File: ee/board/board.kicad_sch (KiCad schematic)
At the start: 53 parts, among them J1 Conn_02x05_Odd_Even, J2 USB_A, J3 Micro_SD_Card_Det_Hirose_DM3AT, J4 Conn_01x08_Pin, J5 Conn_01x10_Pin, J6 Conn_Coaxial, SW1 SW_Push, U2 JW5211, U3 JW5211, U4 F1C100s, U5 SST26VF080A-104I/SN, U6 USBLC6-2SC6, Y1 Crystal_GND24

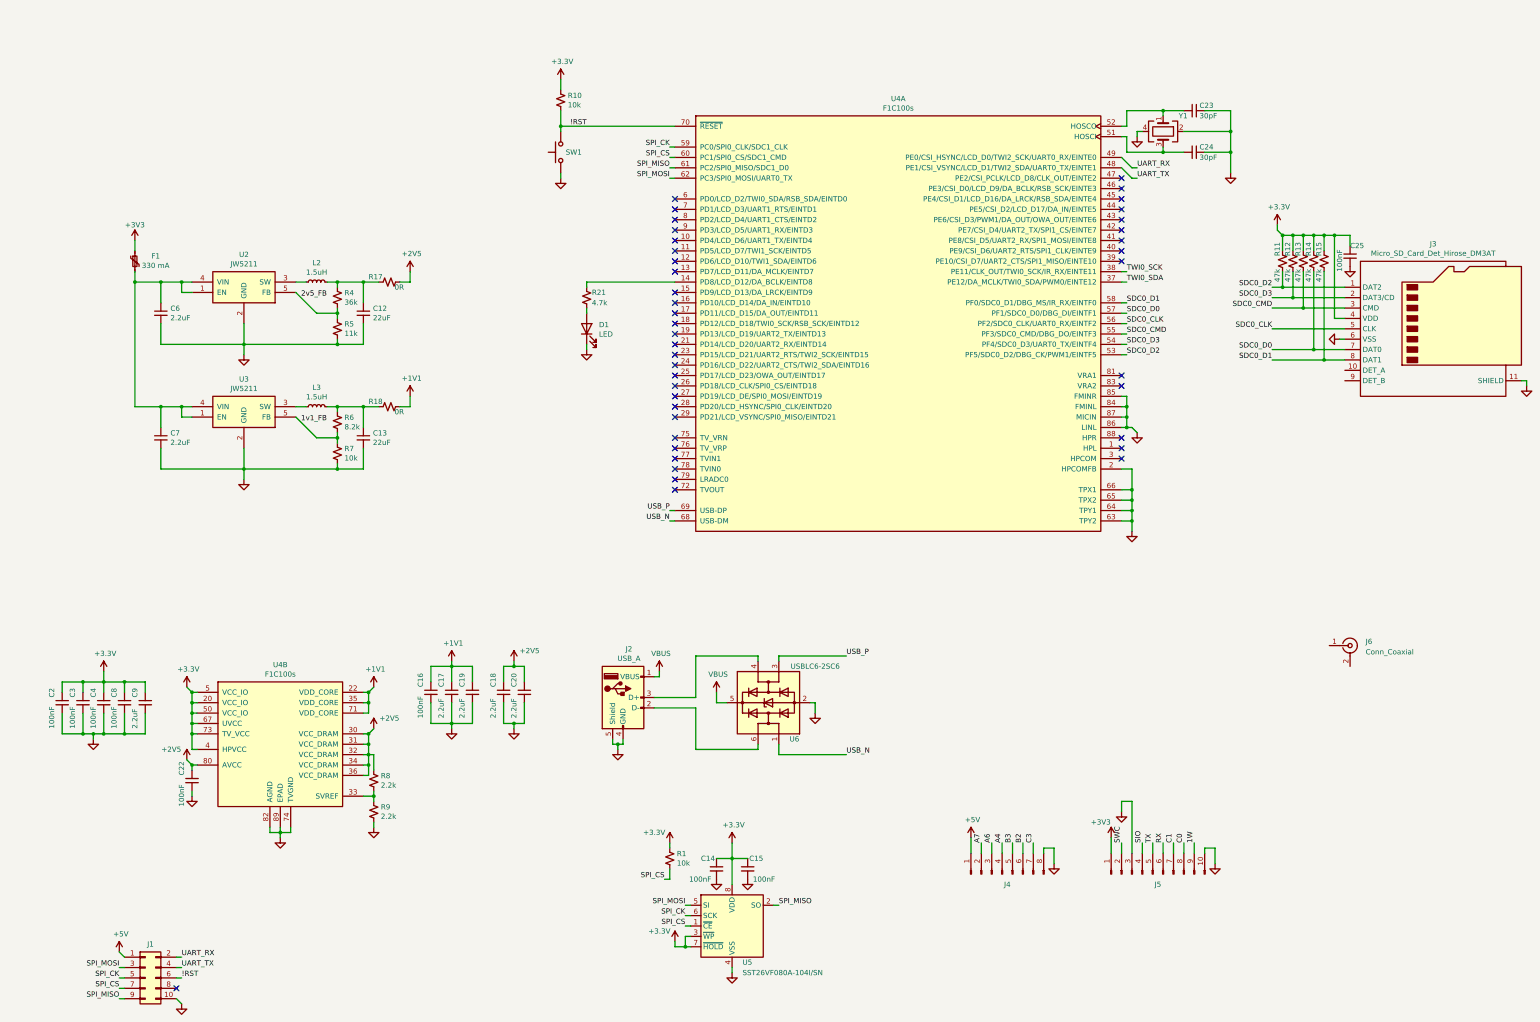
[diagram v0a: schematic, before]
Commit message: Dropped in the M.2 connectors.
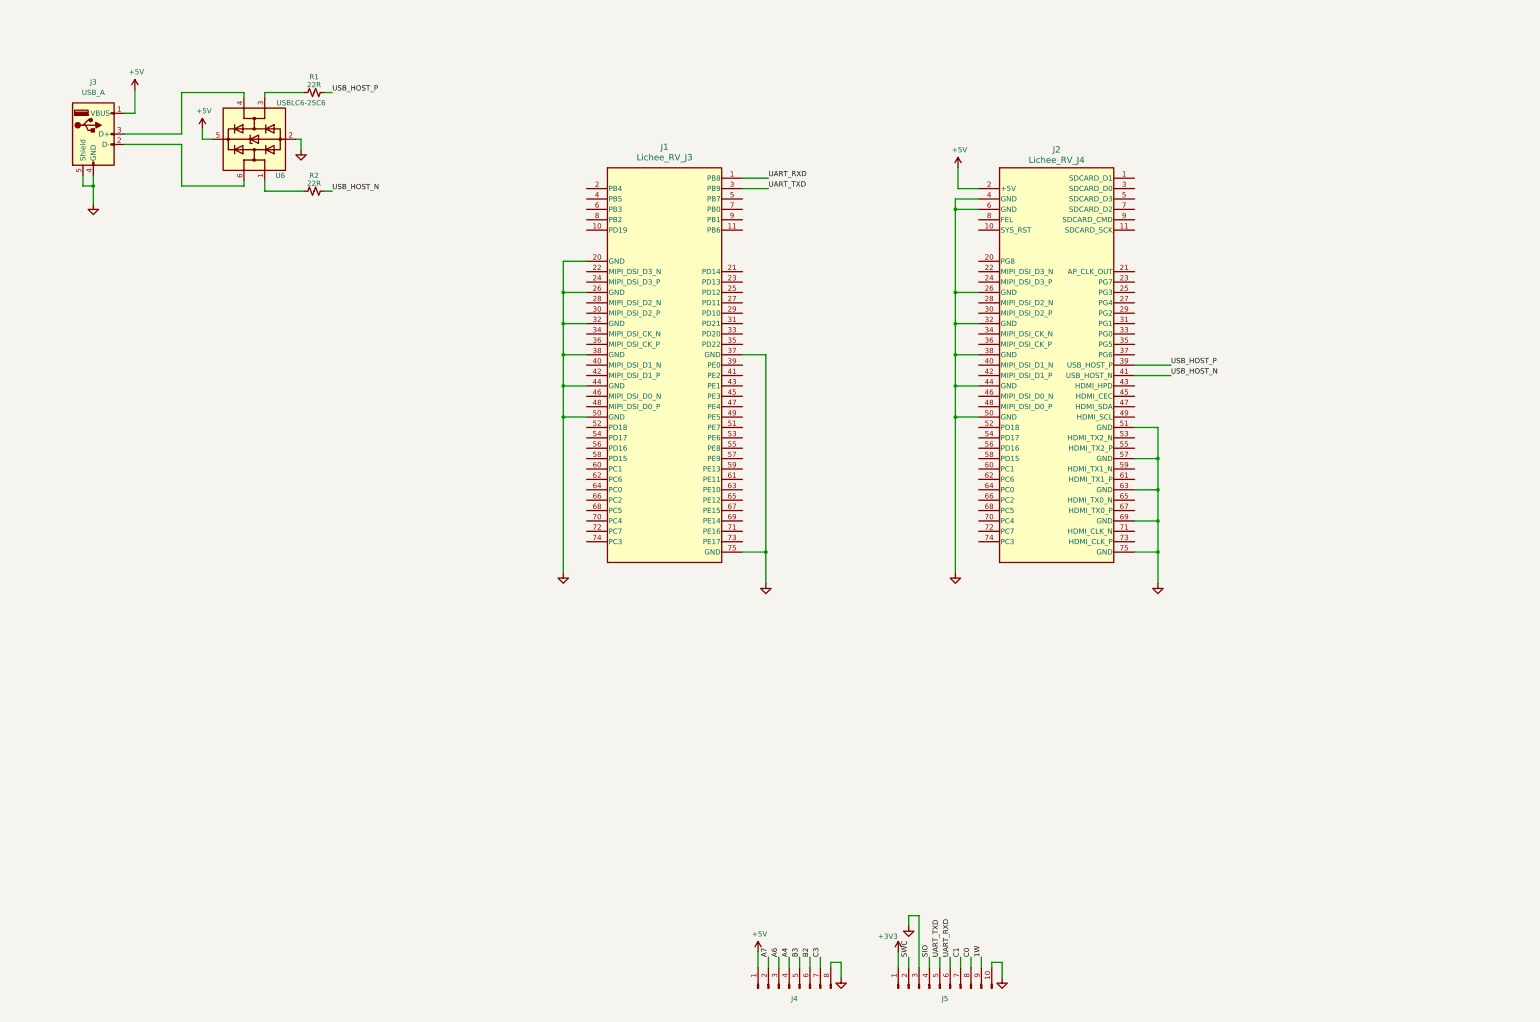
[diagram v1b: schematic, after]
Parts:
- removed C12, C13: 22uF, Capacitor_SMD:C_0805_2012Metric, symbol Device:C_Small
- removed C14, C15, C16, C2, C22, C25, C3, C4, C8: 100nF, Capacitor_SMD:C_0603_1608Metric, symbol Device:C_Small
- removed C17, C18, C19, C20, C6, C7, C9: 2.2uF, Capacitor_SMD:C_0603_1608Metric, symbol Device:C_Small
- removed C23, C24: 30pF, Capacitor_SMD:C_0603_1608Metric, symbol Device:C_Small
- removed D1: LED, LED_SMD:LED_0603_1608Metric, symbol Device:LED
- removed F1: 330 mA, Fuse:Fuse_0603_1608Metric, symbol Device:Polyfuse_Small
- removed J1: Conn_02x05_Odd_Even, Connector_PinSocket_2.54mm:PinSocket_2x05_P2.54mm_Vertical, symbol Connector_Generic:Conn_02x05_Odd_Even
- removed J2: USB_A, Connector_USB:USB_A_Molex_67643_Horizontal, symbol Connector:USB_A
- removed J3: Micro_SD_Card_Det_Hirose_DM3AT, Connector_Card:microSD_HC_Hirose_DM3AT-SF-PEJM5, symbol Connector:Micro_SD_Card_Det_Hirose_DM3AT
- removed J6: Conn_Coaxial, Connector_Coaxial:SMA_Molex_73251-2120_EdgeMount_Horizontal, symbol Connector:Conn_Coaxial
- removed L2, L3: 1.5uH, Inductor_SMD:L_1008_2520Metric, symbol Device:L_Small
- removed R10, R7: 10k, Resistor_SMD:R_0603_1608Metric, symbol Device:R_Small_US
- removed R11, R12, R13, R14, R15: 47k, Resistor_SMD:R_0603_1608Metric, symbol Device:R_Small_US
- removed R17, R18: 0R, Resistor_SMD:R_0603_1608Metric, symbol Device:R_Small_US
- removed R21: 4.7k, Resistor_SMD:R_0603_1608Metric, symbol Device:R_Small_US
- removed R4: 36k, Resistor_SMD:R_0603_1608Metric, symbol Device:R_Small_US
- removed R5: 11k, Resistor_SMD:R_0603_1608Metric, symbol Device:R_Small_US
- removed R6: 8.2k, Resistor_SMD:R_0603_1608Metric, symbol Device:R_Small_US
- removed R8, R9: 2.2k, Resistor_SMD:R_0603_1608Metric, symbol Device:R_Small_US
- removed SW1: SW_Push, Button_Switch_SMD:SW_SPST_TL3342, symbol Switch:SW_Push
- removed U2, U3: JW5211, Package_TO_SOT_SMD:SOT-23-5, symbol board-rescue:JW5211-3340_kicad
- removed U4: F1C100s, 3340:QFN-88_EP_10x10_Pitch0.4mm, symbol board-rescue:F1C100s-3340_kicad
- removed U5: SST26VF080A-104I/SN, Package_SO:SOIC-8_5.275x5.275mm_P1.27mm, symbol board-rescue:SST25VF080B-50-4x-S2Ax-Memory_Flash
- removed Y1: Crystal_GND24, Crystal:Crystal_SMD_Abracon_ABM8G-4Pin_3.2x2.5mm, symbol Device:Crystal_GND24
- added J1: Lichee_RV_J3, 2199119-5:CONN75_2199119-5_TEC, symbol lichee_rv_m2:Lichee_RV_J3
- added J2: Lichee_RV_J4, 2199119-5:CONN75_2199119-5_TEC, symbol lichee_rv_m2:Lichee_RV_J4
- added J3: USB_A, symbol Connector:USB_A
- added R2: 22R, Resistor_SMD:R_0603_1608Metric, symbol Device:R_Small_US
- R1: value 10k -> 22R; MPN RC0603FR-0710KL -> (none)
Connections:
- net VBUS is gone; now on net +5V: U6.5 (VBUS)
- net +3V3: no longer R1.1
- net +5V: now also J2.2 (+5V), J3.1 (VBUS)
- net GND: now also J1.20 (GND), J1.26 (GND), J1.32 (GND), J1.37 (GND), J1.38 (GND), J1.44 (GND), J1.50 (GND), J1.75 (GND), J2.26 (GND), J2.32 (GND), J2.38 (GND), J2.4 (GND), J2.44 (GND), J2.50 (GND), J2.51 (GND), J2.57 (GND), J2.6 (GND), J2.63 (GND), J2.69 (GND), J2.75 (GND), J3.4 (GND), J3.5 (Shield)
- net at U6.6 (I/O1): now also J3.2 (D-)
- net at U6.4 (I/O2): now also J3.3 (D+)
- net RX renamed UART_RXD
- net UART_RXD: now also J1.1 (PB8)
- net SPI_CS renamed USB_HOST_P
- net USB_HOST_P: now also J2.39 (USB_HOST_P)
- net TX renamed UART_TXD
- net UART_TXD: now also J1.3 (PB9)
- net USB_N: no longer names the net of U6.1 (I/O1)
- net USB_N: now also R2.1
- net USB_P: no longer names the net of U6.3 (I/O2)
- net USB_P: now also R1.1
- new net USB_HOST_N: J2.41 (USB_HOST_N), R2.2
- no-connect marks 42 -> 0
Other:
- moved on the sheet: J4, J5, U6

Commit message: Added in module
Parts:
- J3: footprint (none) -> Connector_USB:USB_A_Receptacle_GCT_USB1046; MPN (none) -> USB1046-GF-0190-L-B-A
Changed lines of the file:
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@@
       (effects (font (size 1.27 1.27)))
     )
-    (property "Footprint" "" (at 36.83 47.625 0)
+    (property "Footprint" "Connector_USB:USB_A_Receptacle_GCT_USB1046" (at 36.83 47.625 0)
       (effects (font (size 1.27 1.27)) hide)
     )
@@
       (effects (font (size 1.27 1.27)) hide)
     )
+    (property "MPN" "USB1046-GF-0190-L-B-A" (at 33.02 46.355 0)
+      (effects (font (size 1.27 1.27)) hide)
+    )

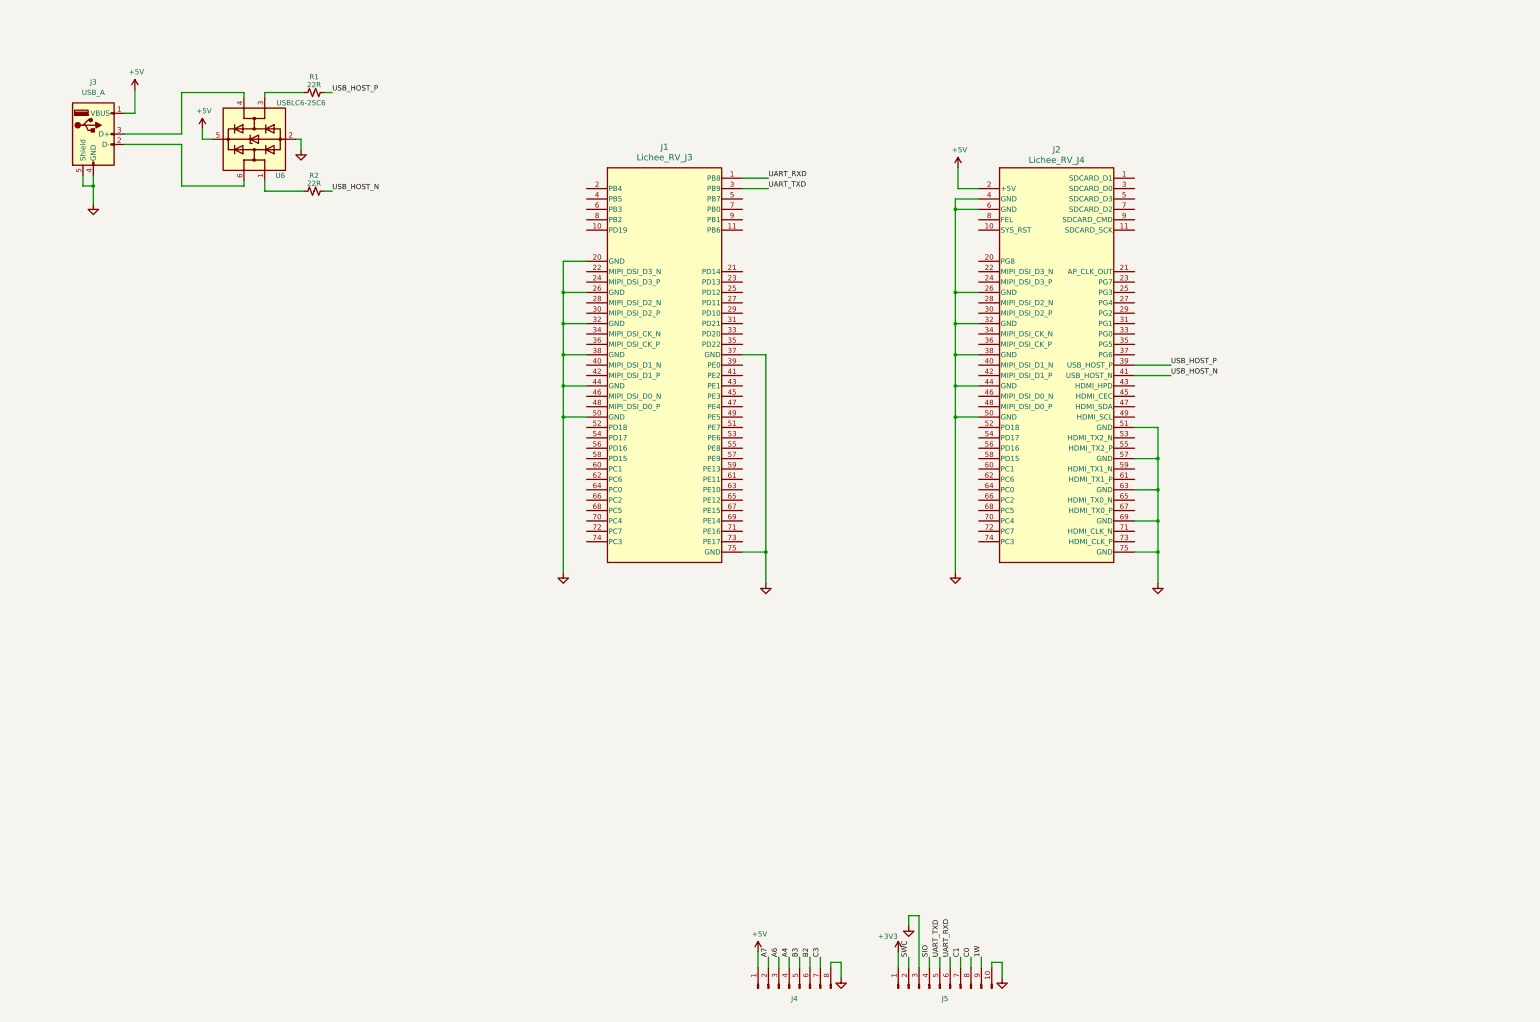
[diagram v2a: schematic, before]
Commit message: Added the wifi module
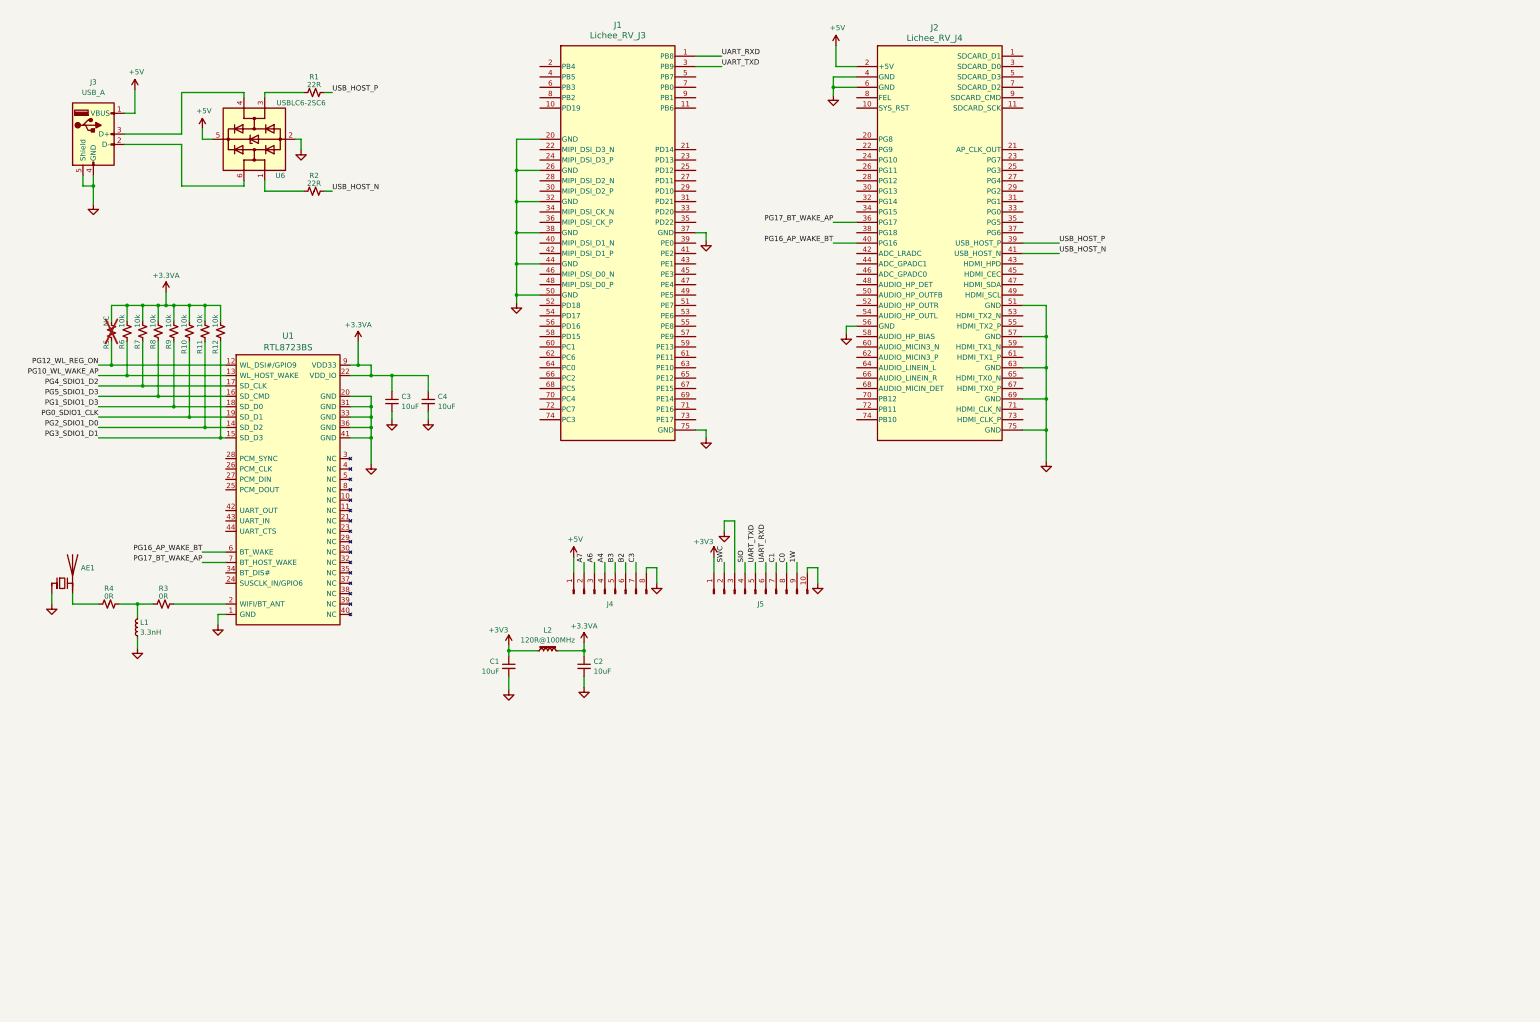
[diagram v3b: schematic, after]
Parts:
- added AE1: Antenna_Chip, symbol Device:Antenna_Chip
- added C1, C2, C3, C4: 10uF, symbol Device:C_Small
- added L1: 3.3nH, symbol Device:L_Small
- added L2: 120R@100MHz, symbol Device:L_Ferrite_Small
- added R10, R11, R12, R6, R7, R8, R9: 10k, Resistor_SMD:R_0603_1608Metric, symbol Device:R_Small_US
- added R3, R4: 0R, Resistor_SMD:R_0603_1608Metric, symbol Device:R_Small_US
- added R5: NC, Resistor_SMD:R_0603_1608Metric, symbol Device:R_Small_US
- added U1: RTL8723BS, Omlex_IC:RL-SM02BD(RTL8723BS), symbol olimex:RTL8723BS(ComboModule)
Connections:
- net +3V3: now also C1.1, L2.1
- net GND: now also J2.56 (GND), AE1.1 (FEED), C1.2, C2.2, C3.2, C4.2, L1.2, U1.1 (GND), U1.20 (GND), U1.31 (GND), U1.33 (GND), U1.36 (GND), U1.41 (GND); no longer J2.26 (GND), J2.32 (GND), J2.38 (GND), J2.44 (GND), J2.50 (GND)
- net PG17_BT_WAKE_AP: now reaches J2.36 (PG17)
- net PG17_BT_WAKE_AP: now also U1.7 (BT_HOST_WAKE)
- net PG16_AP_WAKE_BT: now reaches J2.40 (PG16)
- net PG16_AP_WAKE_BT: now also U1.6 (BT_WAKE)
- new net: R3.2, U1.2 (WIFI/BT_ANT)
- new net: L1.1, R3.1, R4.2
- new net: AE1.2 (PCB_Trace), R4.1
- new net +3.3VA: C2.1, C3.1, C4.1, L2.2, R10.2, R11.2, R12.2, R5.2, R6.2, R7.2, R8.2, R9.2, U1.22 (VDD_IO), U1.9 (VDD33)
- new net PG0_SDIO1_CLK: R10.1, U1.19 (SD_D1)
- new net PG10_WL_WAKE_AP: R6.1, U1.13 (WL_HOST_WAKE)
- new net PG12_WL_REG_ON: R5.1, U1.12 (WL_DSI#/GPIO9)
- new net PG1_SDIO1_D3: R9.1, U1.18 (SD_D0)
- new net PG2_SDIO1_D0: R11.1, U1.14 (SD_D2)
- new net PG3_SDIO1_D1: R12.1, U1.15 (SD_D3)
- new net PG4_SDIO1_D2: R7.1, U1.17 (SD_CLK)
- new net PG5_SDIO1_D3: R8.1, U1.16 (SD_CMD)
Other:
- moved on the sheet: J1, J2, J4, J5
